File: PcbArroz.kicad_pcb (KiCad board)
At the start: 4 copper layers, 88 x 33 mm, 71 parts, among them J1 Conn_Coaxial_Small, J2 USB_C_Receptacle_USB2.0_16P, Q2 SS8050, Q3 AO3400A, Q4 SS8050, SW1 SW_Push, SW2 SW_SPST, U1 ESP32-PICO-D4, U2 RFM95W-915S2, U3 TPS62A01ADRL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

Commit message: pads, gerbers, logo ucu, iniciales y fecha
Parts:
- added UCU: LOGO, logos:LogoUCU, B.Cu at (261.0, 144.2)
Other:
- board text added: "Sensor V1 28/10/2025 CK, RDT, IR"
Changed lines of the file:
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@@
 		(pcbplotparams
 			(layerselection 0x00000000_00000000_55555555_57555fff)
-			(plot_on_all_layers_selection 0x00000000_00000000_00000000_00000000)
+			(plot_on_all_layers_selection 0x00000000_00000000_00000000_020000f5)
 			(disableapertmacros no)
 			(usegerberextensions no)
@@
 		)
 		(fp_text user "${REFERENCE}"
-			(at 0 3.5 0)
+			(at 0.0986 3.0628 0)
 			(layer "F.Fab")
 			(effects
@@
 		)
 	)
+	(footprint "logos:LogoUCU"
+		(layer "B.Cu")
+		(at 260.968963 144.177173 -90)
+		(property "Reference" "UCU"
+			(at 0.05 -8.1 90)
+			(layer "B.SilkS")
+			(effects
+				(font
+					(size 1.5 1.5)
+					(thickness 0.3)
+				)
+				(justify mirror)
+			)
+		)
+		(property "Value" "LOGO"
+			(at 0.75 0 90)
+			(layer "B.SilkS")
+			(hide yes)
+			(effects
+				(font
+					(size 1.5 1.5)
+					(thickness 0.3)
+				)
+				(justify mirror)
+			)
+		)
+		(property "Datasheet" ""
+			(at 0 0 90)
+			(layer "B.Fab")
+			(hide yes)
+			(effects
+				(font
+					(size 1.27 1.27)
+					(thickness 0.15)
+				)
+				(justify mirror)
+			)
+		)
+		(property "Description" ""
+			(at 0 0 90)
+			(layer "B.Fab")
+			(hide yes)
+			(effects
+				(font
+					(size 1.27 1.27)
+					(thickness 0.15)
+				)
+				(justify mirror)
+			)
+		)
+		(attr board_only exclude_from_pos_files exclude_from_bom)
+		(fp_poly
+			(pts
+				(xy 2.3373 -2.758355) (xy 2.733561 -2.760947) (xy 3.021189 -2.764901) (xy 3.184806 -2.770163) (xy 3.217247 -2.774079)
+				(xy 3.207261 -2.853397) (xy 3.149163 -3.025655) (xy 3.084729 -3.184556) (xy 2.921401 -3.564223)
+				(xy 0.022162 -3.564223) (xy -2.877078 -3.564223) (xy -3.058272 -3.173167) (xy -3.239466 -2.782111)
+				(xy -0.026515 -2.762689) (xy 0.650498 -2.759293) (xy 1.28039 -2.757474) (xy 1.847784 -2.75718)
+			)
+			(stroke
+				(width 0)
+				(type solid)
+			)
+			(fill yes)
+			(layer "B.SilkS")
+		)
+		(fp_poly
+			(pts
+				(xy 0.545913 -4.236901) (xy 1.061841 -4.239504) (xy 1.508698 -4.243818) (xy 1.8685 -4.249591) (xy 2.123263 -4.256573)
+				(xy 2.255005 -4.264511) (xy 2.269365 -4.268269) (xy 2.207819 -4.343321) (xy 2.047038 -4.46022) (xy 1.822806 -4.597862)
+				(xy 1.57091 -4.735147) (xy 1.327135 -4.85097) (xy 1.190076 -4.90472) (xy 0.692202 -5.027061) (xy 0.132557 -5.086177)
+				(xy -0.413124 -5.076158) (xy -0.63562 -5.047227) (xy -0.986709 -4.955333) (xy -1.382172 -4.805015)
+				(xy -1.76296 -4.622302) (xy -2.070024 -4.433229) (xy -2.125356 -4.39048) (xy -2.311573 -4.237916)
+				(xy -0.021104 -4.23626)
+			)
+			(stroke
+				(width 0)
+				(type solid)
+			)
+			(fill yes)
+			(layer "B.SilkS")
+		)
+		(fp_poly
+			(pts
+				(xy 0.258221 2.841643) (xy 0.258221 2.469209) (xy 0.630655 2.469209) (xy 1.003089 2.469209) (xy 1.003089 2.208505)
+				(xy 1.003089 1.947801) (xy 0.630655 1.947801) (xy 0.258221 1.947801) (xy 0.258221 1.575367) (xy 0.258221 1.202933)
+				(xy -0.002482 1.202933) (xy -0.263186 1.202933) (xy -0.263186 1.575367) (xy -0.263186 1.947801)
+				(xy -0.598377 1.947801) (xy -0.804333 1.953366) (xy -0.901859 1.991085) (xy -0.9315 2.09249) (xy -0.933568 2.208505)
+				(xy -0.926412 2.368692) (xy -0.877917 2.444547) (xy -0.747538 2.4676) (xy -0.598377 2.469209) (xy -0.263186 2.469209)
+				(xy -0.263186 2.841643) (xy -0.263186 3.214077) (xy -0.002482 3.214077) (xy 0.258221 3.214077)
+			)
+			(stroke
+				(width 0)
+				(type solid)
+			)
+			(fill yes)
+			(layer "B.SilkS")
+		)
+		(fp_poly
+			(pts
+				(xy 0.083367 -0.09892) (xy 0.266292 -0.197452) (xy 0.534923 -0.346635) (xy 0.867829 -0.534168) (xy 1.243578 -0.747748)
+				(xy 1.640739 -0.975074) (xy 2.037882 -1.203843) (xy 2.413574 -1.421754) (xy 2.746386 -1.616503)
+				(xy 3.014886 -1.775789) (xy 3.197643 -1.88731) (xy 3.271213 -1.936772) (xy 3.214105 -1.949787) (xy 3.022496 -1.961899)
+				(xy 2.710855 -1.972828) (xy 2.293652 -1.982295) (xy 1.785359 -1.99002) (xy 1.200445 -1.995722) (xy 0.55338 -1.999124)
+				(xy 0 -2) (xy -0.68814 -1.9994) (xy -1.327158 -1.997682) (xy -1.90235 -1.99497) (xy -2.399012 -1.991389)
+				(xy -2.80244 -1.987062) (xy -3.09793 -1.982114) (xy -3.270777 -1.976667) (xy -3.310938 -1.972089)
+				(xy -3.230782 -1.920019) (xy -3.044529 -1.807997) (xy -2.773306 -1.648176) (xy -2.438239 -1.452707)
+				(xy -2.060454 -1.233742) (xy -1.661079 -1.003432) (xy -1.26124 -0.773928) (xy -0.882062 -0.557383)
+				(xy -0.544673 -0.365947) (xy -0.270199 -0.211773) (xy -0.079766 -0.107012) (xy 0.005499 -0.063814)
+				(xy 0.007578 -0.063343)
+			)
+			(stroke
+				(width 0)
+				(type solid)
+			)
+			(fill yes)
+			(layer "B.SilkS")
+		)
+		(fp_poly
+			(pts
+				(xy 0.826085 5.433003) (xy 1.56645 5.242791) (xy 2.27009 4.936252) (xy 2.923233 4.51762) (xy 3.512113 3.991129)
+				(xy 4.022958 3.361011) (xy 4.442 2.631502) (xy 4.639594 2.158941) (xy 4.83916 1.61261) (xy 4.83916 -0.58475)
+				(xy 4.83916 -2.782111) (xy 4.639594 -3.328442) (xy 4.273832 -4.130371) (xy 3.802406 -4.836361) (xy 3.235564 -5.438682)
+				(xy 2.583557 -5.929606) (xy 1.856634 -6.301401) (xy 1.065044 -6.54634) (xy 0.226769 -6.656327) (xy -0.342579 -6.655542)
+				(xy -0.859287 -6.601281) (xy -0.964491 -6.58143) (xy -1.742803 -6.345104) (xy -2.468076 -5.979174)
+				(xy -3.12561 -5.497994) (xy -3.700703 -4.915916) (xy -4.178653 -4.247293) (xy -4.544758 -3.506479)
+				(xy -4.741703 -2.893841) (xy -4.777662 -2.665668) (xy -4.806352 -2.316189) (xy -4.827762 -1.872893)
+				(xy -4.841884 -1.363271) (xy -4.848706 -0.814813) (xy -4.848391 -0.452726) (xy -3.923259 -0.452726)
+				(xy -3.920778 -1.008001) (xy -3.908867 -1.541615) (xy -3.887526 -2.025175) (xy -3.856753 -2.430295)
+				(xy -3.816551 -2.728583) (xy -3.794205 -2.824457) (xy -3.51721 -3.518744) (xy -3.121275 -4.148303)
+				(xy -2.623726 -4.695883) (xy -2.041893 -5.144233) (xy -1.393103 -5.476101) (xy -0.999688 -5.60661)
+				(xy -0.585767 -5.681085) (xy -0.097356 -5.713174) (xy 0.40158 -5.70257) (xy 0.847074 -5.64897) (xy 0.993334 -5.616129)
+				(xy 1.598566 -5.405653) (xy 2.131601 -5.10615) (xy 2.63619 -4.691772) (xy 2.754803 -4.575502) (xy 3.098371 -4.204003)
+				(xy 3.37393 -3.840824) (xy 3.588328 -3.463707) (xy 3.748412 -3.050394) (xy 3.86103 -2.578629) (xy 3.933029 -2.026154)
+				(xy 3.971257 -1.370711) (xy 3.982561 -0.590043) (xy 3.982562 -0.58475) (xy 3.971403 0.196765) (xy 3.933364 0.852918)
+				(xy 3.861596 1.405965) (xy 3.749252 1.878164) (xy 3.589484 2.291771) (xy 3.375445 2.669045) (xy 3.100287 3.032242)
+				(xy 2.757163 3.403619) (xy 2.754803 3.406001) (xy 2.182801 3.897333) (xy 1.575042 4.247613) (xy 0.916016 4.463379)
+				(xy 0.190212 4.551171) (xy 0.031789 4.553955) (xy -0.720082 4.483976) (xy -1.427987 4.278818) (xy -2.077666 3.949287)
+				(xy -2.654862 3.506185) (xy -3.145318 2.960315) (xy -3.534774 2.322481) (xy -3.794205 1.654956)
+				(xy -3.838877 1.417211) (xy -3.874118 1.059181) (xy -3.899929 0.609255) (xy -3.916309 0.095823)
+				(xy -3.923259 -0.452726) (xy -4.848391 -0.452726) (xy -4.848219 -0.25501) (xy -4.840412 0.288649)
+				(xy -4.825276 0.788673) (xy -4.802801 1.217573) (xy -4.772976 1.547857) (xy -4.743394 1.72434) (xy -4.514242 2.402543)
+				(xy -4.172851 3.071969) (xy -3.744303 3.694039) (xy -3.25368 4.230175) (xy -2.944711 4.490972) (xy -2.227253 4.945902)
+				(xy -1.477676 5.263337) (xy -0.709747 5.447509) (xy 0.062763 5.502653)
+			)
+			(stroke
+				(width 0)
+				(type solid)
+			)
+			(fill yes)
+			(layer "B.SilkS")
+		)
+		(embedded_fonts no)
+	)
 	(footprint "Library:PinSocket_1x04_P2.54mm_Vertical"
 		(layer "B.Cu")
@@
 		)
 	)
+	(gr_text "Sensor V1 28/10/2025\n	CK, RDT, IR"
+		(at 274.3982 135.0284 90)
+		(layer "B.SilkS")
+		(effects
+			(font
+				(size 1 1)
+				(thickness 0.2)
+				(bold yes)
+			)
+			(justify left bottom mirror)
+		)
+	)

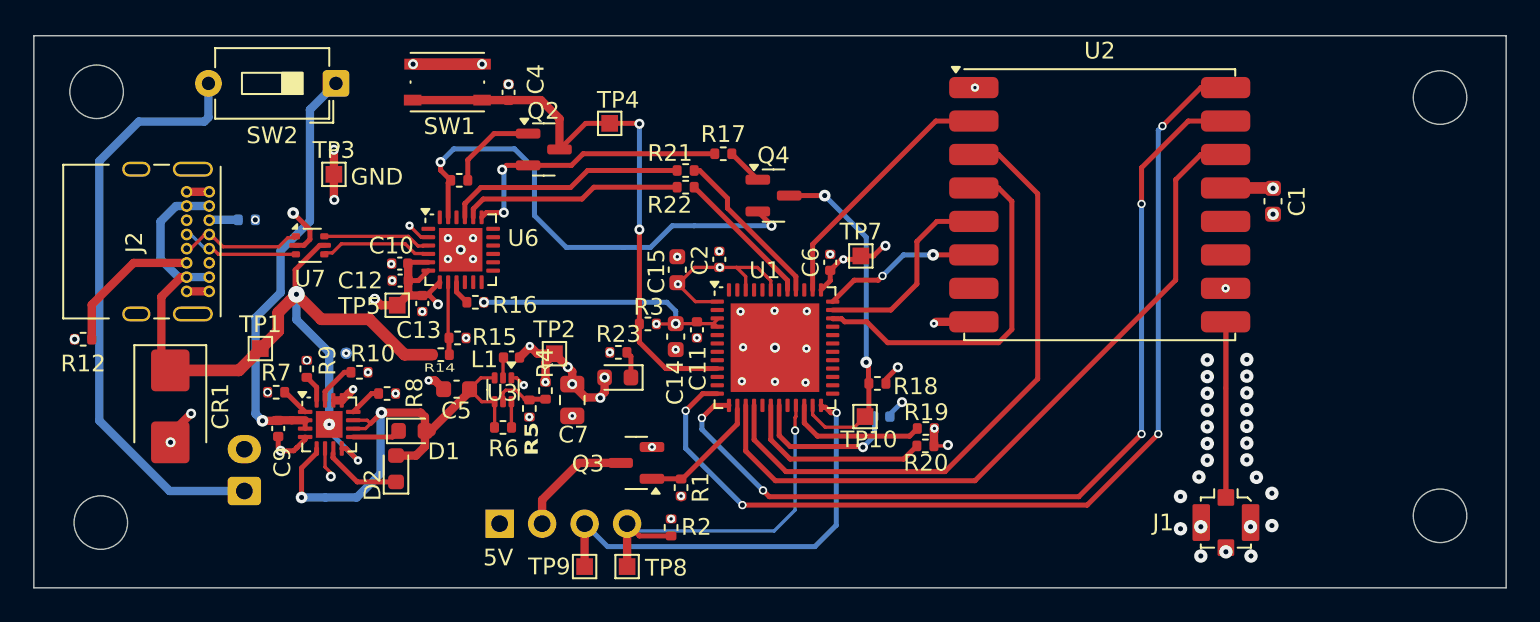
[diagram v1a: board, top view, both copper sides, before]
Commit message: correcciones drc
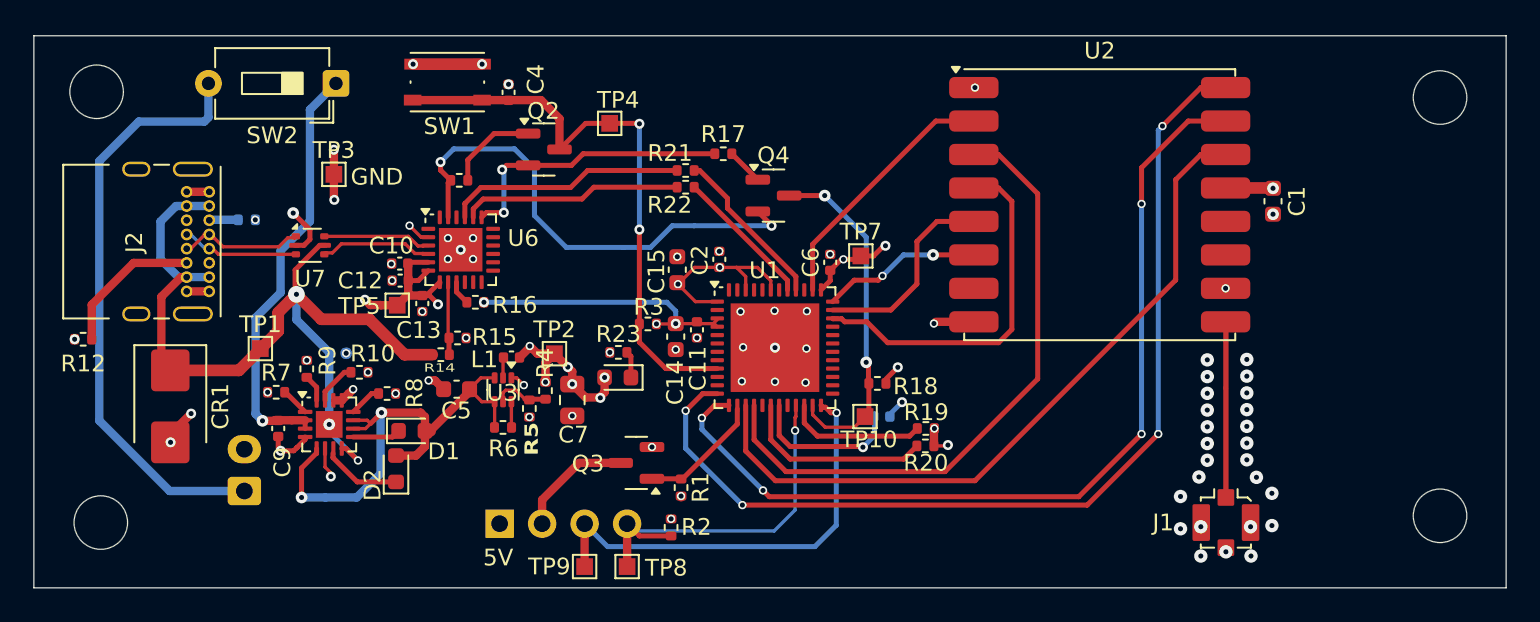
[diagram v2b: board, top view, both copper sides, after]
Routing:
- net +3.3V: track 67.5 -> 68.1 mm, vias 19 -> 18
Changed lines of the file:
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@@
 		(at 233.8344 144.3502)
 		(size 0.5)
-		(drill 0.2)
+		(drill 0.3)
 		(layers "F.Cu" "B.Cu")
 		(net 5)
@@
 		(at 226.316 155.4012)
 		(size 0.5)
-		(drill 0.2)
+		(drill 0.3)
 		(layers "F.Cu" "B.Cu")
 		(net 5)
@@
 		(at 212.3818 139.9846)
 		(size 0.5)
-		(drill 0.2)
+		(drill 0.3)
 		(layers "F.Cu" "B.Cu")
 		(net 5)
@@
 		(at 229.872 144.3756)
 		(size 0.5)
-		(drill 0.2)
+		(drill 0.3)
 		(layers "F.Cu" "B.Cu")
 		(net 5)
@@
 		(at 241.4564 151.3606)
 		(size 0.5)
-		(drill 0.2)
+		(drill 0.3)
 		(layers "F.Cu" "B.Cu")
 		(net 5)
@@
 		(at 230.0244 146.5092)
 		(size 0.5)
-		(drill 0.2)
+		(drill 0.3)
 		(layers "F.Cu" "B.Cu")
 		(net 5)
@@
 		(at 231.904 144.3248)
 		(size 0.5)
-		(drill 0.2)
+		(drill 0.3)
 		(layers "F.Cu" "B.Cu")
 		(net 5)
@@
 		(at 213.8818 139.9846)
 		(size 0.5)
-		(drill 0.2)
+		(drill 0.3)
 		(layers "F.Cu" "B.Cu")
 		(net 5)
@@
 		(at 226.0898 141.0948)
 		(size 0.5)
-		(drill 0.2)
+		(drill 0.3)
 		(layers "F.Cu" "B.Cu")
 		(net 5)
@@
 		(at 209.2556 149.2715)
 		(size 0.5)
-		(drill 0.2)
+		(drill 0.3)
 		(layers "F.Cu" "B.Cu")
 		(net 5)
@@
 		(at 213.8818 141.2346)
 		(size 0.5)
-		(drill 0.2)
+		(drill 0.3)
 		(layers "F.Cu" "B.Cu")
 		(net 5)
@@
 		(at 225.996 146.6448)
 		(size 0.5)
-		(drill 0.2)
+		(drill 0.3)
 		(layers "F.Cu" "B.Cu")
 		(free yes)
@@
 		(at 233.809 146.5854)
 		(size 0.5)
-		(drill 0.2)
+		(drill 0.3)
 		(layers "F.Cu" "B.Cu")
 		(net 5)
@@
 		(at 224.5769 152.4692)
 		(size 0.5)
-		(drill 0.2)
+		(drill 0.3)
 		(layers "F.Cu" "B.Cu")
 		(free yes)
@@
 		(at 233.7582 148.6174)
 		(size 0.5)
-		(drill 0.2)
+		(drill 0.3)
 		(layers "F.Cu" "B.Cu")
 		(net 5)
@@
 		(at 213.4656 145.9504)
 		(size 0.5)
-		(drill 0.2)
+		(drill 0.3)
 		(layers "F.Cu" "B.Cu")
 		(net 5)
@@
 		(at 229.9482 148.5412)
 		(size 0.5)
-		(drill 0.2)
+		(drill 0.3)
 		(layers "F.Cu" "B.Cu")
 		(net 5)
@@
 		(at 210.085002 139.2346)
 		(size 0.5)
-		(drill 0.2)
+		(drill 0.3)
 		(layers "F.Cu" "B.Cu")
 		(net 5)
@@
 		(at 207.6046 148.0015)
 		(size 0.5)
-		(drill 0.2)
+		(drill 0.3)
 		(layers "F.Cu" "B.Cu")
 		(net 5)
@@
 		(at 217.2482 150.6768)
 		(size 0.5)
-		(drill 0.2)
+		(drill 0.3)
 		(layers "F.Cu" "B.Cu")
 		(net 5)
@@
 		(at 225.7202 156.7652)
 		(size 0.5)
-		(drill 0.2)
+		(drill 0.3)
 		(layers "F.Cu" "B.Cu")
 		(net 5)
@@
 		(at 227.266 145.9446)
 		(size 0.5)
-		(drill 0.2)
+		(drill 0.3)
 		(layers "F.Cu" "B.Cu")
 		(free yes)
@@
 		(at 235.2314 140.9492)
 		(size 0.5)
-		(drill 0.2)
+		(drill 0.3)
 		(layers "F.Cu" "B.Cu")
 		(net 5)
@@
 		(at 206.7136 149.0175)
 		(size 0.5)
-		(drill 0.2)
+		(drill 0.3)
 		(layers "F.Cu" "B.Cu")
 		(net 5)
@@
 		(at 243.8818 130.9846)
 		(size 0.5)
-		(drill 0.2)
+		(drill 0.3)
 		(layers "F.Cu" "B.Cu")
 		(net 5)
@@
 		(at 228.602 140.7714)
 		(size 0.5)
-		(drill 0.2)
+		(drill 0.3)
 		(layers "F.Cu" "B.Cu")
 		(net 5)
@@
 		(at 206.2982 146.8648)
 		(size 0.5)
-		(drill 0.2)
+		(drill 0.3)
 		(layers "F.Cu" "B.Cu")
 		(net 5)
@@
 		(at 209.0466 142.5214)
 		(size 0.5)
-		(drill 0.2)
+		(drill 0.3)
 		(layers "F.Cu" "B.Cu")
 		(net 5)
@@
 		(at 219.8136 150.6088)
 		(size 0.5)
-		(drill 0.2)
+		(drill 0.3)
 		(layers "F.Cu" "B.Cu")
 		(net 5)
@@
 		(at 258.8648 142.9846)
 		(size 0.5)
-		(drill 0.2)
+		(drill 0.3)
 		(layers "F.Cu" "B.Cu")
 		(net 5)
@@
 		(at 211.2284 148.4904)
 		(size 0.5)
-		(drill 0.2)
+		(drill 0.3)
 		(layers "F.Cu" "B.Cu")
 		(free yes)
@@
 		(at 208.9958 141.5308)
 		(size 0.5)
-		(drill 0.2)
+		(drill 0.3)
 		(layers "F.Cu" "B.Cu")
 		(net 5)
@@
 		(at 222.0588 146.8126)
 		(size 0.5)
-		(drill 0.2)
+		(drill 0.3)
 		(layers "F.Cu" "B.Cu")
 		(net 5)
@@
 		(at 216.91819 148.768613)
 		(size 0.5)
-		(drill 0.2)
+		(drill 0.3)
 		(layers "F.Cu" "B.Cu")
 		(net 5)
@@
 		(at 231.9294 148.5666)
 		(size 0.5)
-		(drill 0.2)
+		(drill 0.3)
 		(layers "F.Cu" "B.Cu")
 		(net 5)
@@
 		(at 241.429 145.0868)
 		(size 0.5)
-		(drill 0.2)
+		(drill 0.3)
 		(layers "F.Cu" "B.Cu")
 		(net 5)
@@
 		(at 212.3818 141.2346)
 		(size 0.5)
-		(drill 0.2)
+		(drill 0.3)
 		(layers "F.Cu" "B.Cu")
 		(net 5)
@@
 		(at 210.8474 144.373)
 		(size 0.5)
-		(drill 0.2)
+		(drill 0.3)
 		(layers "F.Cu" "B.Cu")
 		(net 5)
@@
 	)
 	(segment
+		(start 208.3718 143.9828)
+		(end 208.3836 143.9946)
+		(width 0.5)
+		(layer "F.Cu")
+		(net 7)
+	)
+	(segment
 		(start 228.4798 145.2798)
 		(end 228.2948 145.0948)
@@
 	)
 	(segment
+		(start 207.7368 143.9828)
+		(end 208.3718 143.9828)
+		(width 0.5)
+		(layer "F.Cu")
+		(net 7)
+	)
+	(segment
 		(start 230.8846 141.7346)
 		(end 229.6318 141.7346)
@@
 	)
 	(segment
-		(start 208.3836 143.9946)
-		(end 208.0026 143.6136)
-		(width 0.5)
-		(layer "F.Cu")
-		(net 7)
-	)
-	(segment
 		(start 238.4318 140.4386)
 		(end 237.8222 141.0482)
@@
 	)
 	(segment
-		(start 209.3488 143.9946)
-		(end 208.3836 143.9946)
+		(start 207.4184 143.6644)
+		(end 207.7368 143.9828)
 		(width 0.5)
 		(layer "F.Cu")
@@
 		(net 7)
 	)
+	(segment
+		(start 208.3836 143.9946)
+		(end 209.3488 143.9946)
+		(width 0.5)
+		(layer "F.Cu")
+		(net 7)
+	)
 	(via
 		(at 237.1872 152.4782)
@@
 		(at 217.2736 146.433)
 		(size 0.5)
-		(drill 0.2)
+		(drill 0.3)
 		(layers "F.Cu" "B.Cu")
 		(net 7)
@@
 		(at 224.8448 145.1122)
 		(size 0.5)
-		(drill 0.2)
+		(drill 0.3)
 		(layers "F.Cu" "B.Cu")
 		(net 7)
@@
 		(at 236.0188 141.2514)
 		(size 0.5)
-		(drill 0.2)
+		(drill 0.3)
 		(layers "F.Cu" "B.Cu")
 		(net 7)
@@
 		(at 218.2134 148.59)
 		(size 0.5)
-		(drill 0.2)
+		(drill 0.3)
 		(layers "F.Cu" "B.Cu")
 		(net 7)
@@
 	)
 	(via
-		(at 208.0026 143.6136)
+		(at 207.4184 143.6644)
 		(size 0.6)
 		(drill 0.3)
@@
 	)
 	(via
-		(at 208.0026 143.6136)
-		(size 0.6)
-		(drill 0.3)
-		(layers "F.Cu" "B.Cu")
-		(net 7)
-	)
-	(via
 		(at 226.1318 142.7346)
 		(size 0.5)
-		(drill 0.2)
+		(drill 0.3)
 		(layers "F.Cu" "B.Cu")
 		(net 7)
@@
 		(at 228.6318 141.7346)
 		(size 0.5)
-		(drill 0.2)
+		(drill 0.3)
 		(layers "F.Cu" "B.Cu")
 		(net 7)
@@
 		(at 205.2848 151.1193)
 		(size 0.7)
-		(drill 0.2)
+		(drill 0.3)
 		(layers "F.Cu" "B.Cu")
 		(net 10)
@@
 		(at 207.0057 153.272)
 		(size 0.5)
-		(drill 0.2)
-		(layers "F.Cu" "B.Cu")
-		(net 10)
+		(drill 0.3)
+		(layers "F.Cu" "B.Cu")
+		(net 10)
